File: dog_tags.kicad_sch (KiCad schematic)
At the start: 0 parts

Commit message: smallest schematic ever
Signed-off-by: Lucy Mielke <user@domain.tld>
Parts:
- added AE1: LXMS21ACMD-220, Capacitor_SMD:C_0805_2012Metric_Pad1.18x1.45mm_HandSolder, symbol Device:Antenna_Dipole
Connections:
- new net GND: AE1.1, AE1.2
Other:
- company: (none) -> ${AUTHOR}
- title: (none) -> ${TITLE}

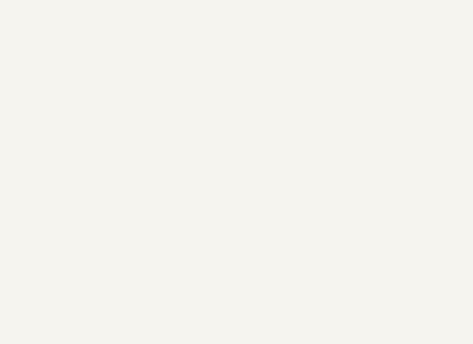
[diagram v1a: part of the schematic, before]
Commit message: add perfboard holes
Signed-off-by: Lucy Mielke <user@domain.tld>
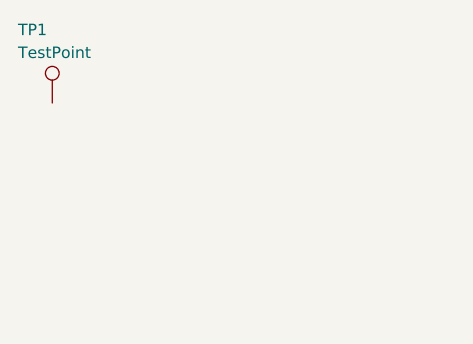
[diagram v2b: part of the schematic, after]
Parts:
- added TP1: TestPoint, Connector_PinSocket_2.54mm:PinSocket_1x01_P2.54mm_Vertical, symbol Connector:TestPoint
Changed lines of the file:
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@@
+	)
+	(symbol
+		(lib_id "Connector:TestPoint")
+		(at 46.99 44.45 0)
+		(unit 1)
+		(body_style 1)
+		(exclude_from_sim no)
+		(in_bom yes)
+		(on_board yes)
+		(in_pos_files yes)
+		(dnp no)
+		(property "Reference" "TP1"
+			(at 43.18 36.322 0)
+			(show_name no)
+			(do_not_autoplace no)
+			(effects
+				(font
+					(size 1.27 1.27)
+				)
+				(justify left)
+			)
+		)
+		(property "Value" "TestPoint"
+			(at 43.18 38.862 0)
+			(show_name no)
+			(do_not_autoplace no)
+			(effects
+				(font
+					(size 1.27 1.27)
+				)
+				(justify left)
+			)
+		)
+		(property "Footprint" "Connector_PinSocket_2.54mm:PinSocket_1x01_P2.54mm_Vertical"
+			(at 52.07 44.45 0)
+			(hide yes)
+			(show_name no)
+			(do_not_autoplace no)
+			(effects
+				(font
+					(size 1.27 1.27)
+				)
+			)
+		)
+		(property "Datasheet" ""
+			(at 52.07 44.45 0)
+			(hide yes)
+			(show_name no)
+			(do_not_autoplace no)
+			(effects
+				(font
+					(size 1.27 1.27)
+				)
+			)
+		)
+		(property "Description" "test point"
+			(at 46.99 44.45 0)
+			(hide yes)
+			(show_name no)
+			(do_not_autoplace no)
+			(effects
+				(font
+					(size 1.27 1.27)
+				)
+			)
+		)
+		(pin "1"
+		)
+		(instances
+			(project "dog_tags"
+				(path "/4c0635ca-6983-4c8f-ae7e-16ab10cb4f8b"
+					(reference "TP1")
+					(unit 1)
+				)
+			)
+		)
 	)
 	(symbol
